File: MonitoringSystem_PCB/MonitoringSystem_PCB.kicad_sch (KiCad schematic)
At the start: 8 parts

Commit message: delete
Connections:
- net at U?.1 (ENABLE): now also U?.42 (GPIO21)
- net at U?.10 (DIN): now also U?.36 (GPIO23)
- net at U?.12 (SCLK): now also U?.35 (GPIO18)
- net VDD: now reaches U?.14 (VDD)
- net VDD: now also J?.1 (Vcc), U?.1 (VDDA_1)
- net at U?.3 (START): now also U?.39 (GPIO22)
- net at U?.4 (STOP): now also U?.34 (GPIO5)
- net GND: now reaches U?.7 (GND)
- net GND: now also J?.3 (GND)
- net at U?.9 (DOUT): now also U?.38 (GPIO19)
- net at J?.2 (Signal): now also U?.14 (GPIO25)
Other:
- moved on the sheet: J?, U?

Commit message: schematic updates
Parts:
- removed J?: 1050171001, CON00679_5_MOL, symbol micro-usb_connector:1050171001
- removed U?: LM1117-3.3, symbol Regulator_Linear:LM1117-3.3
- removed U?: CP2102N-A02-GQFN20R, QFN20_SIL, symbol CP2102-GMR:CP2102N-A02-GQFN20R
- removed U?: ESP32-U4WDH, symbol ESP32-U4WDH:ESP32-U4WDH
- added C4, C7: 1u, Capacitor_SMD:C_0805_2012Metric, symbol basic:C
- added C5: 100 uF, symbol Device:C_Small
- added C6: 0.1 uF, symbol Device:C_Small
- added J1: Ultrasonic_Conn_2, symbol Connector_Generic:Conn_01x03
- added JP1: SolderJumper_3_Open, Jumper:SolderJumper-3_P2.0mm_Open_TrianglePad1.0x1.5mm, symbol Jumper:SolderJumper_3_Open
- added R3, R4: 100k, Resistor_SMD:R_0805_2012Metric, symbol basic:R
- added R5: 1k, Resistor_SMD:R_0805_2012Metric, symbol basic:R
- added SW1, SW2: SW_Push, Button_Switch_SMD:SW_SPST_B3S-1000, symbol Switch:SW_Push
- added U2: ESP32-S3-WROOM-1-N16R2, local_footprints:ESP32-S3-WROOM-1_EXP, symbol local_symbols:ESP32-S3-WROOM-1-N16R2
- added U3: NC7SZ157P6X, SOIC_Z157P6X_ONS, symbol 2-to-1_MUX:NC7SZ157P6X
- J?: value Ultrasonic_Conn -> Ultrasonic_Conn_1
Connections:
- net GND: now also C4.2, C5.2, C6.2, C7.2, J1.3 (GND), JP1.1 (A), SW1.1, SW2.1, U2.40 (GND), U2.41 (GND), U2.42 (GND), U2.43 (GND), U2.44 (GND), U2.45 (GND), U2.46 (GND), U2.47 (GND), U2.48 (GND), U2.49 (GND); no longer U?.7 (GND)
- net Signal_1: now reaches J?.2 (Signal)
- net VDD: no longer names the net of U?.14 (VDD)
- net VDD: no longer J?.1 (Vcc)
- new net: JP1.2 (C), R5.2
- new net +3.3V: C5.1, C6.1, J1.1 (Vcc), J?.1 (Vcc), U2.2 (3V3)
- new net +3V3: JP1.3 (B), R3.1, R4.1
- new net CHIP_PU: C4.1, R3.2, SW1.2, U2.3 (EN)
- new net GPIO0_STRAPPING: C7.1, R4.2, SW2.2, U2.27 (IO0)
- new net GPIO3_STRAPPING: R5.1, U2.15 (IO3)
- new net RX: U2.37 (TXD0)
- new net Signal_2: J1.2 (Signal)
- new net TX: U2.36 (RXD0)
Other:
- added sheet Power_Programming_Circuit (Power_Programming.kicad_sch)
- moved on the sheet: J?, U?

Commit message: finish first draft of schematic of PCB
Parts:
- removed J1: Ultrasonic_Conn_2, symbol Connector_Generic:Conn_01x03
- removed J?: Ultrasonic_Conn_1, symbol Connector_Generic:Conn_01x03
- removed U3: NC7SZ157P6X, SOIC_Z157P6X_ONS, symbol 2-to-1_MUX:NC7SZ157P6X
- removed U?: TDC7200PW, PW0014A_N, symbol time-to-DC:TDC7200PW
- removed U?: OPA192ID, D14_TEX, symbol op-amp OPA192ID:OPA192ID
- added C23, C26: 2.2 uF, symbol Device:C_Small
- added C24, C25: 1 uF, symbol Device:C_Small
- added J4: Conn_ARM_JTAG_SWD_10, Connector_IDC:IDC-Header_2x05_P2.54mm_Vertical, symbol Connector:Conn_ARM_JTAG_SWD_10
- added JP2: SolderJumper_3_Open, Jumper:SolderJumper-3_P2.0mm_Open_TrianglePad1.0x1.5mm, symbol Jumper:SolderJumper_3_Open
- added JP3: SolderJumper_2_Open, Jumper:SolderJumper-2_P1.3mm_Open_TrianglePad1.0x1.5mm, symbol Jumper:SolderJumper_2_Open
- added R10: 66.67k, Resistor_SMD:R_0805_2012Metric, symbol basic:R
- added R11, R12, R13: 4.7k, Resistor_SMD:R_0805_2012Metric, symbol basic:R
- added R6, R9: 1k, Resistor_SMD:R_0805_2012Metric, symbol basic:R
- added TP1, TP2, TP3, TP4, TP5, TP6: TestPoint, symbol Connector:TestPoint
- C5: value 100 uF -> 10 uF
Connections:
- net +3V3 is gone; now on net +3.3V: JP1.3 (B), R3.1, R4.1
- net +3.3V: now also J?.7 (Vdd), C25.1, JP2.3 (B), JP3.1 (A), R11.2, R12.2, R13.2, R6.2
- net CHIP_PU: now also J4.10 (~{RESET})
- net GND: now also J?.6 (Vss), C23.2, C24.2, C25.2, C26.2, J4.3 (GND), J4.5 (GND), J4.9 (GNDDetect), JP2.1 (A), R10.1
- net CLK_OUT3 (8 MHz): now reaches U2.11 (IO18)
- net LCD_CS: now reaches U2.12 (IO8)
- net LCD_CS: now also J?.8 (CS), R11.1, TP4.1
- net GPIO46_STRAPPING: now reaches U2.16 (IO46)
- net GPIO46_STRAPPING: now also R6.1
- net TDC1000_EN: now reaches U2.17 (IO9)
- net TDC1000_RST: now reaches U2.18 (IO10)
- net TDC1000_CHANNEL_SELECT: now reaches U2.19 (IO11)
- net TDC1000_ERRB: now reaches U2.20 (IO12)
- net TDC7200_EN: now reaches U2.21 (IO13)
- net TDC7200_INT: now reaches U2.22 (IO14)
- net SPI_MOSI: now reaches U2.25 (IO48)
- net SPI_MOSI: now also J?.12 (MOSI), TP1.1
- net GPIO45_STRAPPING: now reaches U2.26 (IO45)
- net GPIO45_STRAPPING: now also R9.1
- net SPI_MISO: now reaches U2.28 (IO35)
- net SPI_MISO: now also TP2.1
- net SPI_SCK: now reaches U2.29 (IO36)
- net SPI_SCK: now also J?.11 (SCLK), TP3.1
- net TDC7200_CS: now reaches U2.30 (IO37)
- net TDC7200_CS: now also R13.1, TP6.1
- net TDC1000_CS: now reaches U2.31 (IO38)
- net TDC1000_CS: now also R12.1, TP5.1
- net MTCK: now reaches U2.32 (IO39)
- net MTCK: now also J4.4 (SWDCLK/TCK)
- net MTDO: now reaches U2.33 (IO40)
- net MTDO: now also J4.6 (SWO/TDO)
- net MTDI: now reaches U2.34 (IO41)
- net MTDI: now also J4.8 (NC/TDI)
- net MTMS: now reaches U2.35 (IO42)
- net MTMS: now also J4.2 (SWDIO/TMS)
- net LCD_RST: now reaches U2.8 (IO15)
- net LCD_RST: now also J?.9 (RST)
- net LCD_DATA/CMD: now reaches U2.9 (IO16)
- net LCD_DATA/CMD: now also J?.10 (Data/CMD)
- net at J?.13 (Iref): now also R10.2
- net at J?.14 (Vcomh): now also C26.1
- net +5V: now reaches J?.15 (Vcc)
- net +5V: now also C23.1
- net at J?.5 (Vbat): now also C24.1
- new net: JP2.2 (C), R9.2
- new net: J4.1 (VTref), JP3.2 (B)
- no-connect marks 0 -> 4
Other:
- sheet Power_Programming_Circuit renamed Power and Programming Subsystem
- added sheet Ultrasonic Sensing Subsystem (ultrasonic_sensing_subsytem.kicad_sch)
- sheet Power and Programming Subsystem: file Power_Programming.kicad_sch -> power_programming_subsytem.kicad_sch
- note added: "Debug Header"
- note added: "ESP32-S3-WROOM-N16 Module"
- note added: "LCD Screen Connector"
- moved on the sheet: C4, C7, J?, JP1, R3, R4, SW1, SW2, U2

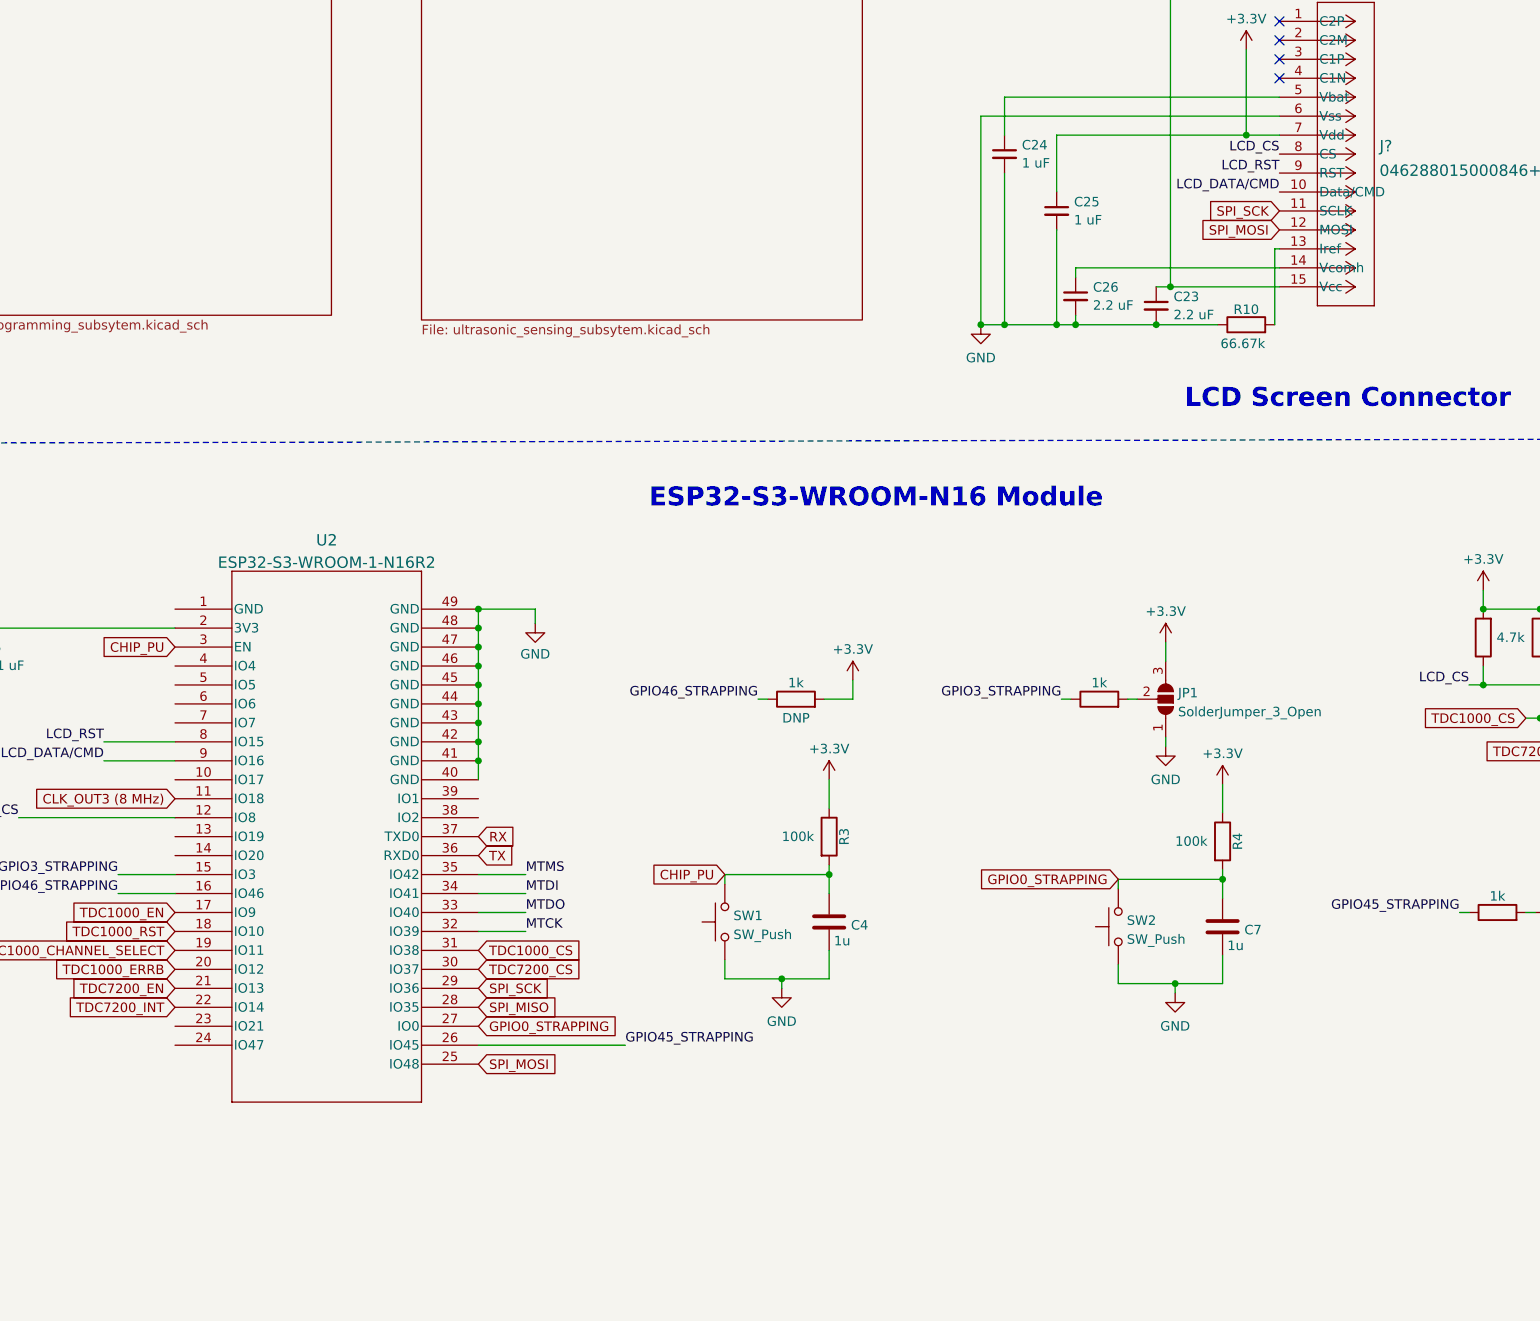
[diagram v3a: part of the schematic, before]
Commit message: switched micro-usb for usb-b, started pcb
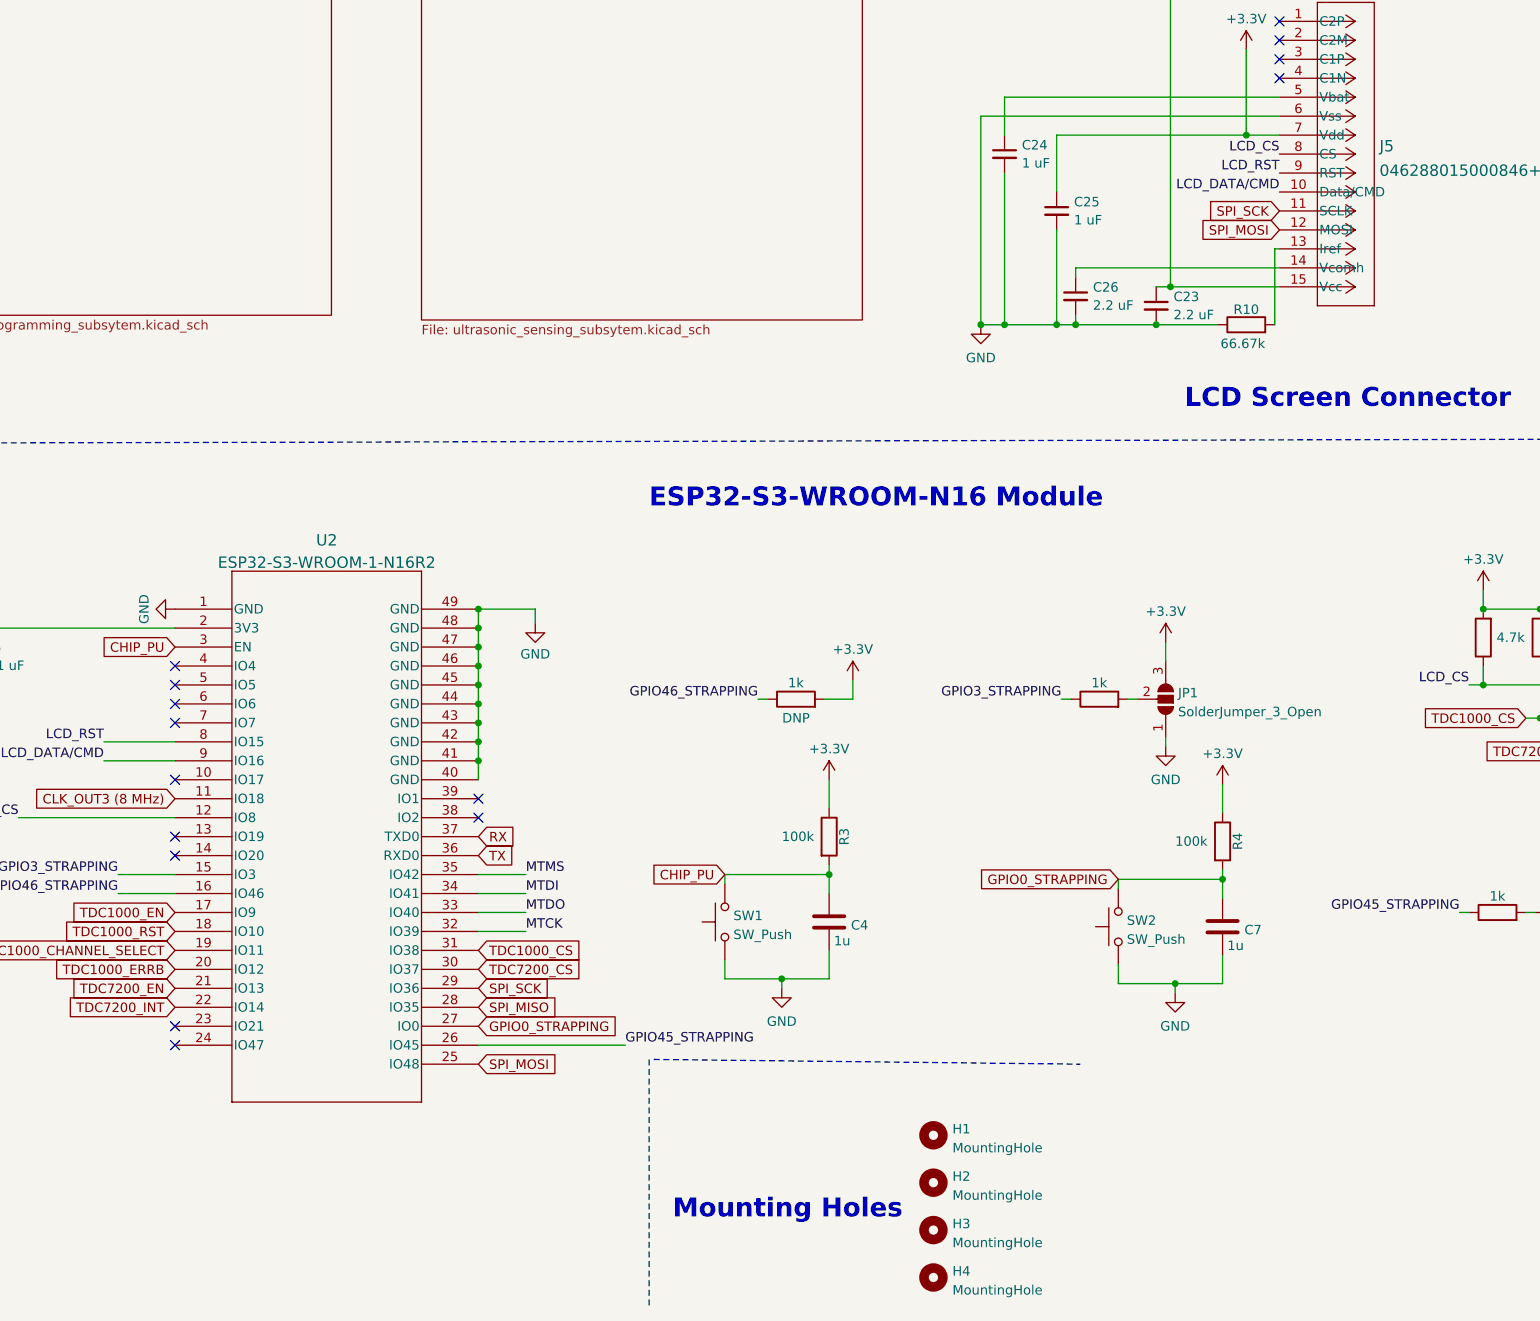
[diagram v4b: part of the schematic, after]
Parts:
- added H1, H2, H3, H4: MountingHole, MountingHole:MountingHole_3.2mm_M3, symbol Mechanical:MountingHole
- C23, C24, C25, C26, C5, C6: footprint (none) -> Capacitor_SMD:C_0805_2012Metric
- J5: renamed from J?; footprint CONN15_6288_7X5P7_AVX -> ZIF_LCD_connector:CONN15_6288_7X5P7_AVX
- TP1, TP2, TP3, TP4, TP5, TP6: footprint (none) -> TestPoint:TestPoint_Keystone_5010-5014_Multipurpose
- U2: footprint local_footprints:ESP32-S3-WROOM-1_EXP -> ESP32-S3-WROOM-N16:ESP32-S3-WROOM-1_EXP
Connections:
- net GND: now also U2.1 (GND)
- no-connect marks 4 -> 15
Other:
- note added: "Mounting Holes"

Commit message: BOM and minor pcb updates
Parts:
- C4, C7: value 1u -> 1 uF
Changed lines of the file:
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@@
 			)
 		)
-		(property "Value" "1u"
+		(property "Value" "1 uF"
 			(at 196.215 148.59 0)
 			(effects
@@
 			)
 		)
-		(property "Value" "1u"
+		(property "Value" "1 uF"
 			(at 143.51 147.955 0)
 			(effects

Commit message: most recent pcb
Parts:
- removed TP1, TP2, TP3, TP4, TP5, TP6: TestPoint, TestPoint:TestPoint_Keystone_5010-5014_Multipurpose, symbol Connector:TestPoint
- added C32: 1 uF, Capacitor_SMD:C_0805_2012Metric, symbol basic:C
- added D6: PAIR_IND, LED_SMD:LED_0805_2012Metric, symbol Device:LED
- added D7: CONN_IND, LED_SMD:LED_0805_2012Metric, symbol Device:LED
- added R19, R20: 1k, Resistor_SMD:R_0805_2012Metric, symbol Device:R
- added R21: 100k, Resistor_SMD:R_0805_2012Metric, symbol basic:R
- added R24, R25, R26, R27: SPI_R, Resistor_SMD:R_0805_2012Metric, symbol Device:R
- added SW3: SW_Push, Button_Switch_SMD:SW_SPST_B3S-1000, symbol Switch:SW_Push
- J5: footprint ZIF_LCD_connector:CONN15_6288_7X5P7_AVX -> ZIF_LCD_connector:15Pin_TAB
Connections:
- net +3.3V: now also R21.1
- net GND: now also C32.2, D6.1 (K), D7.1 (K), SW3.1
- net SPI_MISO: now also U2.30 (IO37); no longer U2.28 (IO35)
- net SPI_MOSI: now also R24.2; no longer U2.25 (IO48)
- net SPI_SCK: now also R27.2; no longer U2.29 (IO36)
- net TDC1000_CS: now also R25.2; no longer U2.31 (IO38)
- net TDC7200_CS: now also R26.2; no longer U2.30 (IO37)
- net SOFT_RST: now reaches U2.4 (IO4)
- net SOFT_RST: now also C32.1, R21.2, SW3.2
- net PAIR_IND: now reaches U2.5 (IO5)
- net PAIR_IND: now also R19.1
- net CONN_IND: now reaches U2.6 (IO6)
- net CONN_IND: now also R20.1
- net CLK_OUT3 (8 MHz) renamed CLK_OUT3 (1 MHz)
- new net: R25.1, U2.31 (IO38)
- new net: D6.2 (A), R19.2
- new net: R26.1, U2.25 (IO48)
- new net: R24.1, U2.28 (IO35)
- new net: R27.1, U2.29 (IO36)
- new net: D7.2 (A), R20.2
- no-connect marks 15 -> 12
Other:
- moved on the sheet: C4, C7, JP1, JP2, R3, R4, SW1, SW2
